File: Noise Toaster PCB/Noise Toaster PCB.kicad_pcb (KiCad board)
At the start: 2 copper layers, 170 x 97.5 mm, 133 parts, among them Q1 2N5457, Q10 2N3906, Q2 2N3904, Q3 2N3904, Q4 2N3904, Q5 2N3904, Q6 2N3904, Q7 2N5457, Q8 2N5457, Q9 2N5457, U1 LM324, U2 LM324, U3 LM386, X10 Conn_01x01_Pin, X11 Conn_01x01_Pin, X12 Conn_01x01_Pin, X13 Conn_01x01_Pin, X14 Conn_01x01_Pin, X24 Conn_01x01_Pin, X25 Conn_01x01_Pin, X26 Conn_01x01_Pin, X27 Conn_01x01_Pin, X8 Conn_01x01_Pin, X9 Conn_01x01_Pin

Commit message: created pcb file
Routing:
- net GND: track 0.00 -> 173.6 mm
- net /ARG: track 0.00 -> 90.3 mm
- net /RMP: track 0.00 -> 88.5 mm
- net /G2: track 0.00 -> 77.0 mm
- net /Attack Release Envelope Generator/X19: track 0.00 -> 73.7 mm
- net /Front Panel/B: track 0.00 -> 73.6 mm
- net /Audio Amplifier/X27: track 0.00 -> 60.0 mm
- net /Front Panel/X10: track 0.00 -> 54.5 mm
- net Net-(R39-Pad2): track 0.00 -> 46.4 mm
- net /SQR: track 0.00 -> 44.5 mm
- net Net-(Q3-C): track 0.00 -> 40.5 mm
- net Net-(U2D-+): track 0.00 -> 40.0 mm
- net /Front Panel/X5: track 0.00 -> 39.9 mm
- net /AA: track 0.00 -> 39.4 mm
- net Net-(Q3-B): track 0.00 -> 39.0 mm
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- added copper zone on F.Cu, net B+
- added copper zone on B.Cu, net B-
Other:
- board size 170 x 97.5 mm -> 168.2 x 96.5 mm

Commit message: created gerber files
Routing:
- net B+: track 37.9 -> 20.0 mm
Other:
- board text added: "Music From Outer Space LLC Design by Ray Wilson CC-BY-NC-SA"
- board text added: "Noise Toaster"
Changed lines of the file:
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@@
       (viasonmask false)
       (mode 1)
-      (useauxorigin false)
+      (useauxorigin true)
       (hpglpennumber 1)
       (hpglpenspeed 20)
@@
       (outputformat 1)
       (mirror false)
-      (drillshape 1)
+      (drillshape 0)
       (scaleselection 1)
-      (outputdirectory "")
+      (outputdirectory "Gerber Files")
     )
   )
@@
   (gr_rect (start 63.84 49.84) (end 232.09 146.34)
     (stroke (width 0.1) (type default)) (fill none) (layer "Edge.Cuts"))
+  (gr_text "Music From Outer Space LLC\nDesign by Ray Wilson\nCC-BY-NC-SA" (at 198.84 144.34) (layer "F.SilkS")
+    (effects (font (size 1 1) (thickness 0.15)) (justify left bottom))
+  )
+  (gr_text "Noise Toaster" (at 73.84 53.34) (layer "F.SilkS")
+    (effects (font (size 2 2) (thickness 0.15)) (justify left bottom))
+  )
   (segment (start 180.2 90.03) (end 175.15 90.03) (width 0.5) (layer "F.Cu") (net 1))
   (segment (start 185.255 100.215) (end 185.28 100.19) (width 0.5) (layer "F.Cu") (net 1))
@@
   (segment (start 187.3 91.3) (end 188.84 92.84) (width 0.5) (layer "F.Cu") (net 7))
   (segment (start 187.795 104.52) (end 187.795 112.14) (width 0.5) (layer "F.Cu") (net 7))
-  (segment (start 190.34 57.34) (end 190.34 57.03) (width 0.5) (layer "F.Cu") (net 8))
-  (segment (start 181.34 63.34) (end 183.34 61.34) (width 0.5) (layer "F.Cu") (net 8))
   (segment (start 179.87 65.52) (end 180.642233 65.52) (width 0.5) (layer "F.Cu") (net 8))
-  (segment (start 180.642233 65.52) (end 181.34 64.822233) (width 0.5) (layer "F.Cu") (net 8))
-  (segment (start 186.34 61.34) (end 190.34 57.34) (width 0.5) (layer "F.Cu") (net 8))
-  (segment (start 183.34 61.34) (end 186.34 61.34) (width 0.5) (layer "F.Cu") (net 8))
-  (segment (start 190.34 57.03) (end 192.9 54.47) (width 0.5) (layer "F.Cu") (net 8))
-  (segment (start 181.34 64.822233) (end 181.34 63.34) (width 0.5) (layer "F.Cu") (net 8))
   (segment (start 107.25 82.82) (end 106 84.07) (width 0.5) (layer "B.Cu") (net 8))
   (segment (start 106 84.07) (end 99.07 84.07) (width 0.5) (layer "B.Cu") (net 8))

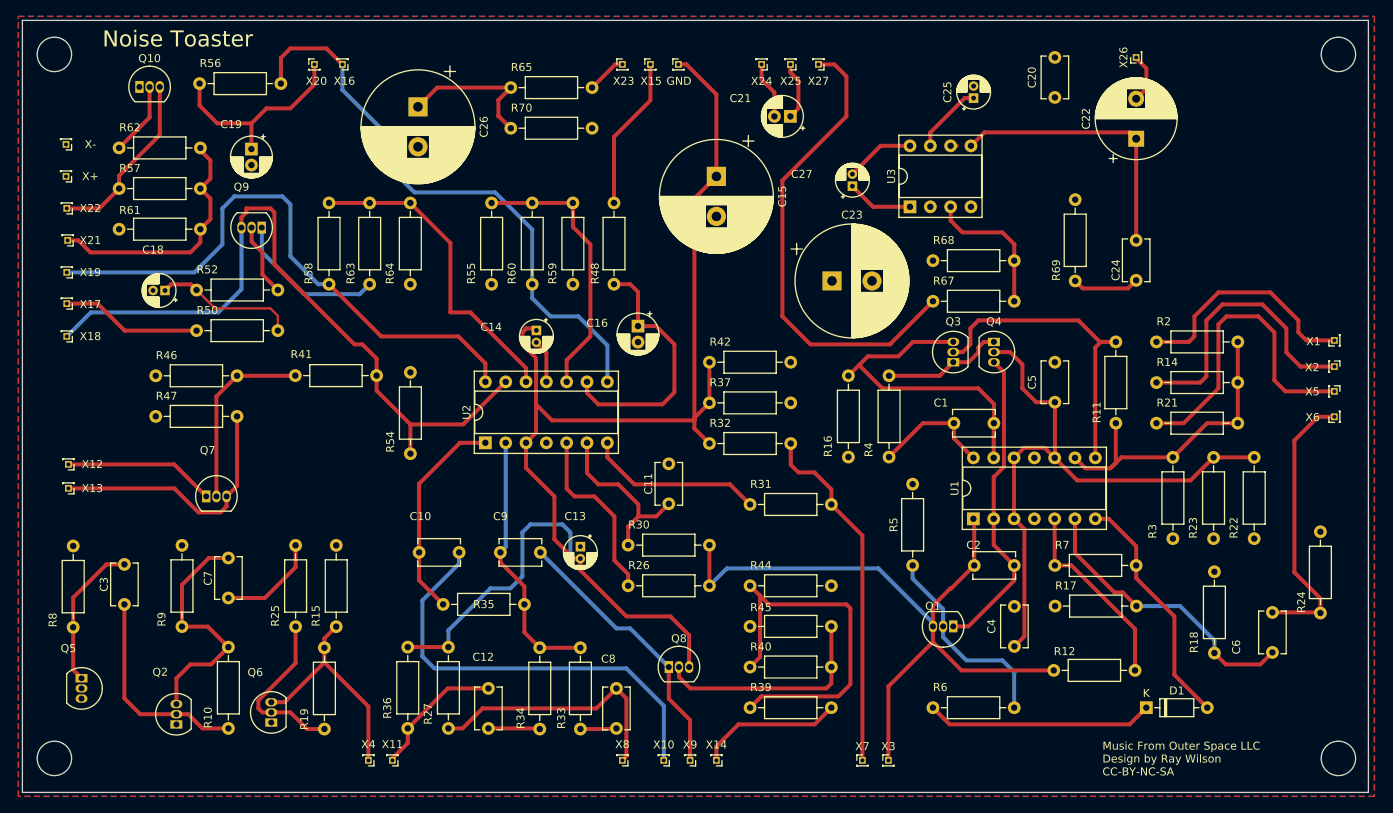
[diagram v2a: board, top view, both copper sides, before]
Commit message: rerooted some circuit paths
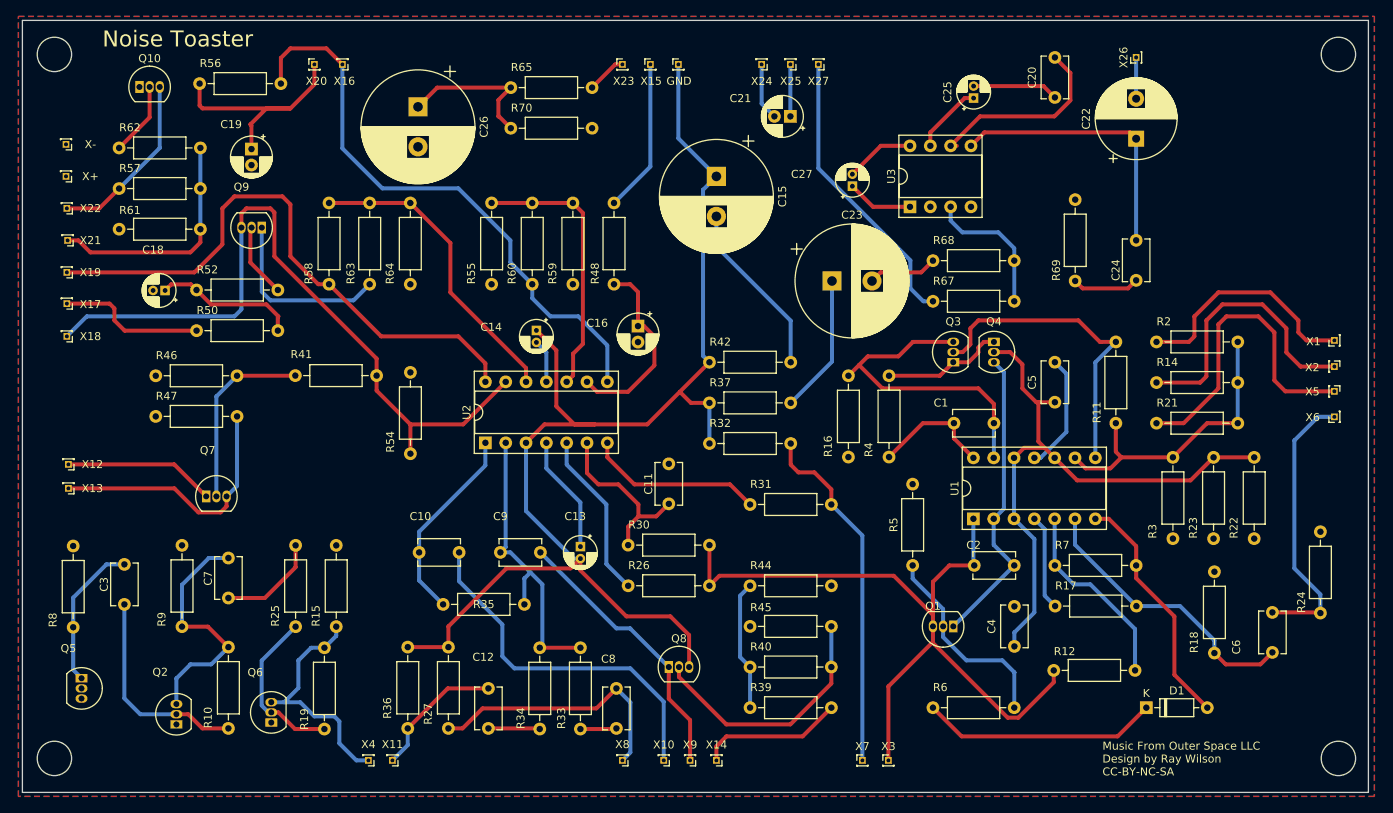
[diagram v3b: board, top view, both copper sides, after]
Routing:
- net B+: track 20.0 -> 91.2 mm
- net B-: track 5.45 -> 61.6 mm
- net Net-(R39-Pad2): track 46.4 -> 16.3 mm
- net /Audio Amplifier/X27: track 60.0 -> 36.3 mm
- net GND: track 173.6 -> 161.2 mm
- net /Front Panel/X10: track 54.5 -> 45.1 mm
- net Net-(U2C--): track 32.7 -> 24.2 mm
- net /RMP: track 88.5 -> 95.1 mm
- net Net-(U2A--): track 33.0 -> 38.3 mm
- net /Front Panel/X20: track 25.7 -> 29.9 mm
- net Net-(Q8-G): track 28.3 -> 32.0 mm
- net /Attack Release Envelope Generator/X21: track 31.9 -> 29.8 mm
- net /FO: track 26.7 -> 24.9 mm
- net /WNS: track 28.5 -> 30.1 mm
- net Net-(U2D-+): track 40.0 -> 38.5 mm
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
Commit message: changed the pcb to the original size factor
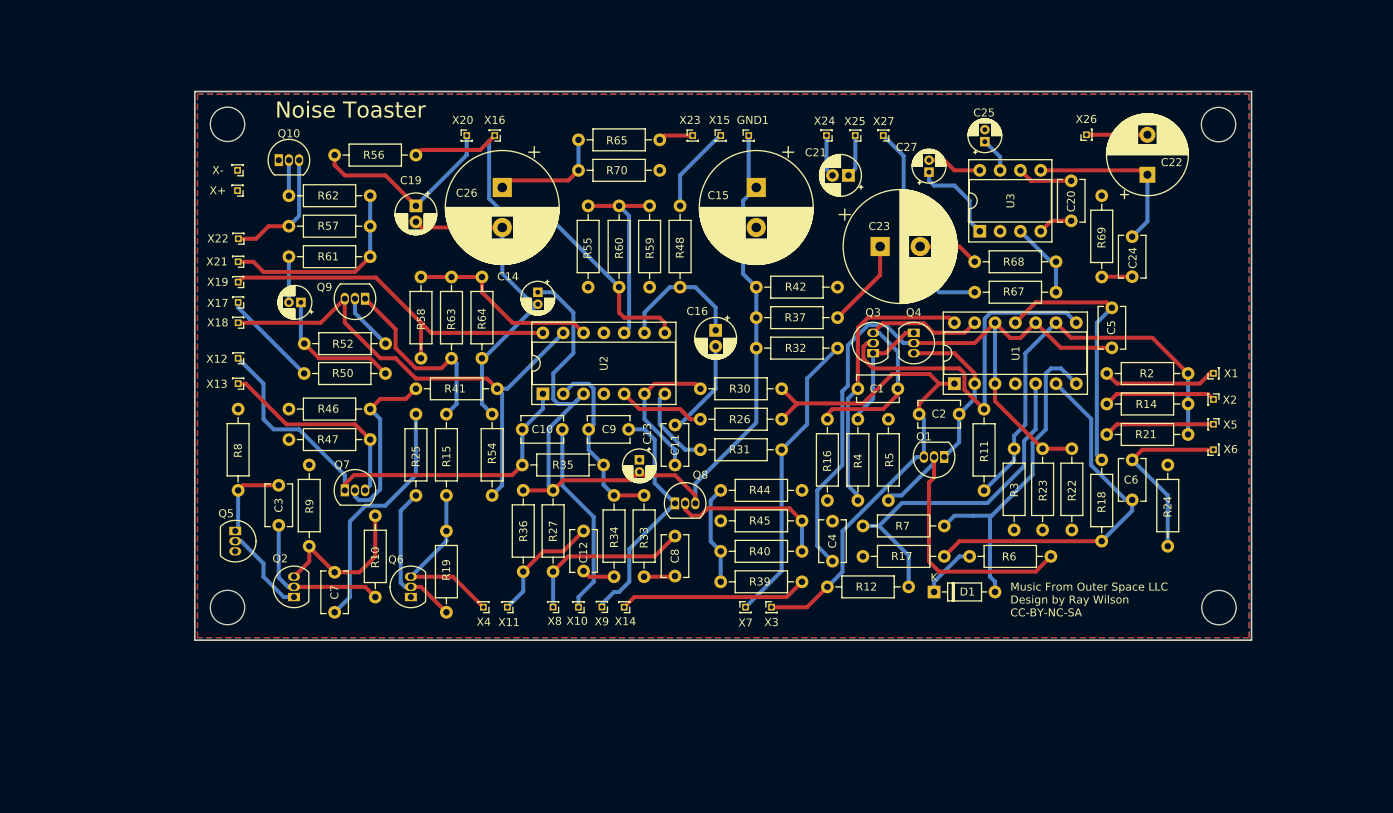
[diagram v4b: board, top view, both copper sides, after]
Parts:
- moved D1 30.2 mm to (177.8, 121.3)
- moved R12 30.2 mm to (164.5, 120.7)
- moved REF** 28.7 mm to (89.5, 123.2)
- moved R8 26.8 mm to (90.8, 98.4)
- moved Q5 26.6 mm to (90.4, 113.7)
- moved C6 25.9 mm to (202.6, 104.8)
- moved C4 25.1 mm to (165.1, 117.4)
- moved X12 25.0 mm to (90.8, 92.1)
- moved X13 24.9 mm to (90.8, 95.2)
- moved R17 24.8 mm to (179.1, 116.8)
- moved R10 24.6 mm to (108.0, 111.8)
- moved R7 24.5 mm to (168.9, 113.0)
- moved R36 24.3 mm to (126.4, 108.6)
- moved X3 24.1 mm to (157.5, 123.2)
- moved X7 24.1 mm to (154.2, 123.2)
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- renumbered GND to GND1
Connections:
- Q7 pad 1: /Front Panel/A -> /FO
- X12 pad 1: /Front Panel/A -> /FO
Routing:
- net B-: track 61.6 -> 116.5 mm
- net GND: track 161.2 -> 110.7 mm
- net B+: track 91.2 -> 42.1 mm
- net /FO: track 24.9 -> 57.8 mm
- net /Attack Release Envelope Generator/X19: track 73.7 -> 45.6 mm
- net /RMP: track 95.1 -> 67.4 mm
- net /Front Panel/X5: track 39.9 -> 13.9 mm
- net /ARG: track 91.1 -> 65.6 mm
- net /Front Panel/B: track 73.2 -> 50.6 mm
- net Net-(D1-K): track 29.6 -> 7.03 mm
- net /Front Panel/X2: track 35.4 -> 14.1 mm
- net /Front Panel/X10: track 45.1 -> 24.6 mm
- net Net-(C1-Pad2): track 15.2 -> 34.8 mm
- net Net-(U1B-+): track 24.4 -> 43.3 mm
- net /Front Panel/A: track 18.9 -> 0.00 mm
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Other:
- board size 168.2 x 96.5 mm -> 132.1 x 68.6 mm

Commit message: beautified pcb
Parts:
- moved C25 19.4 mm to (174.0, 81.5)
- moved C5 19.4 mm to (189.9, 107.3)
- moved D1 19.4 mm to (167.7, 137.8)
- moved Q3 19.4 mm to (160.1, 108.0)
- moved R21 19.4 mm to (199.4, 118.1)
- moved R3 19.4 mm to (177.7, 119.9)
- moved R33 19.4 mm to (131.4, 135.9)
- moved R4 19.4 mm to (158.1, 116.2)
- moved C14 19.4 mm to (118.1, 100.4)
- moved C26 19.4 mm to (113.7, 87.3)
- moved Q7 19.4 mm to (94.0, 125.1)
- moved Q9 19.4 mm to (96.6, 101.2)
- moved R27 19.4 mm to (120.0, 135.3)
- moved R35 19.4 mm to (116.2, 121.9)
- moved R56 19.4 mm to (102.9, 83.2)
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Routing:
- net GND: track 110.7 -> 114.1 mm
- net /Front Panel/B: track 50.6 -> 53.4 mm
- net /Front Panel/X20: track 25.0 -> 27.0 mm
- net /Front Panel/X15: track 11.0 -> 12.9 mm
- net /Audio Amplifier/X24: track 5.30 -> 7.05 mm
- net /Audio Amplifier/X27: track 26.9 -> 28.7 mm
- net /Audio Amplifier/X25: track 5.34 -> 7.08 mm
- net /Front Panel/X23: track 4.34 -> 5.88 mm
- net /Audio Amplifier/X26: track 7.62 -> 9.05 mm

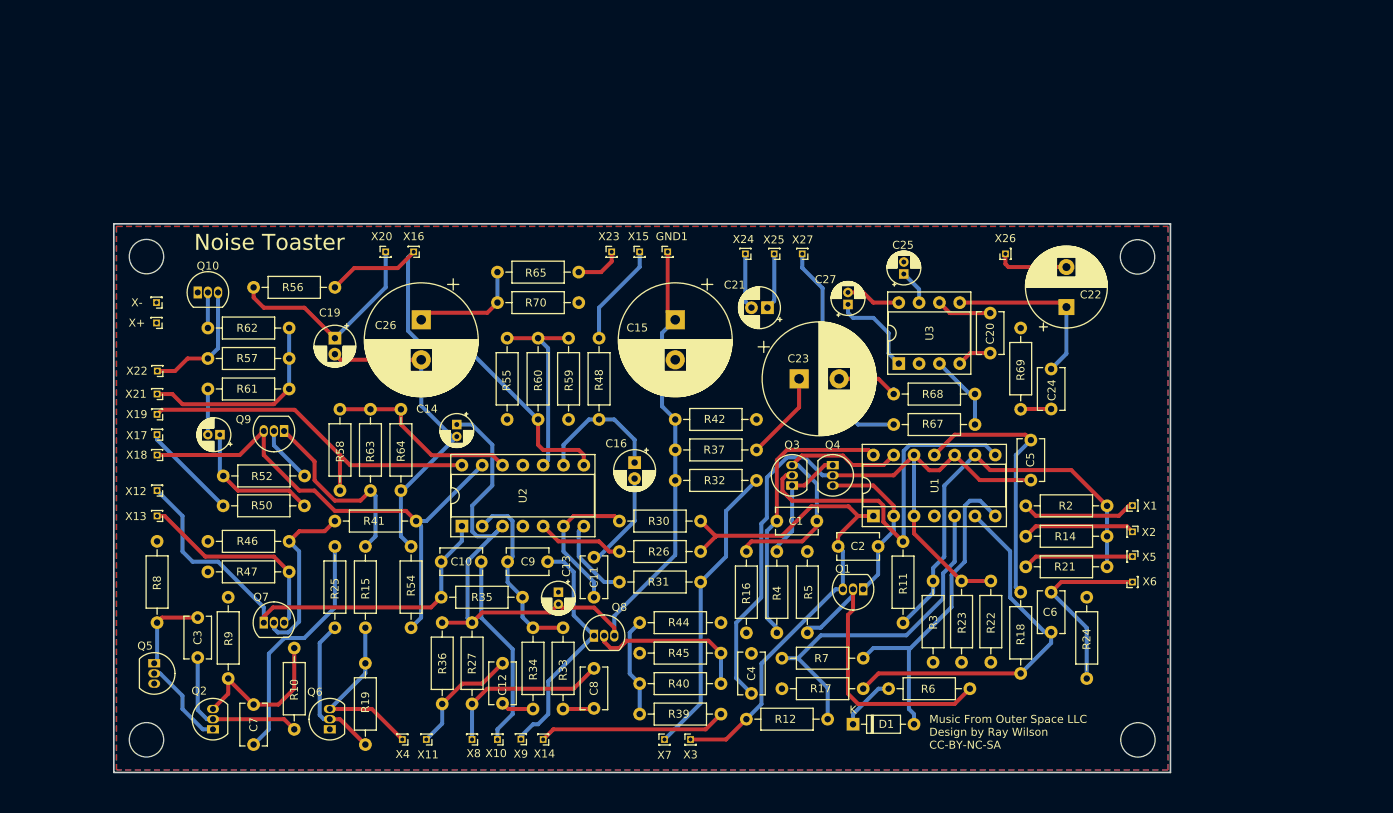
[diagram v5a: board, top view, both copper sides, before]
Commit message: changed header pins to groups
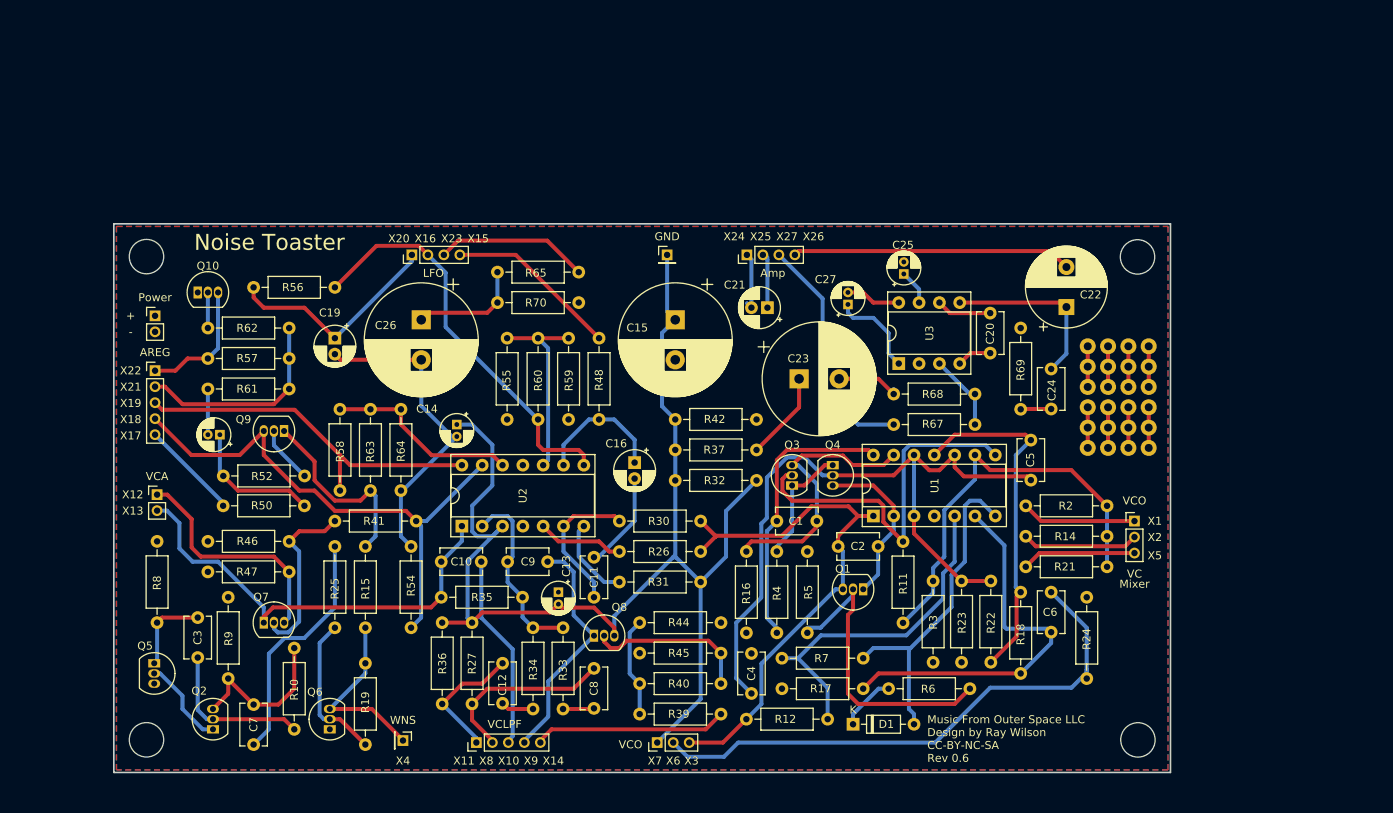
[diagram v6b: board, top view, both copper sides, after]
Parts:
- removed X+, X-, X1, X15, X16, X17, X18, X19, X2, X20, X21, X22, X23, X3, X5, X6, X7: ~, Connector_PinHeader_1.00mm:PinHeader_1x01_P1.00mm_Vertical
- removed X10, X11, X12, X13, X14, X24, X25, X26, X27, X8, X9: Conn_01x01_Pin, Connector_PinHeader_1.00mm:PinHeader_1x01_P1.00mm_Vertical
- added ?: , , F.Cu at (202.1, 103.3)
- added ?: , , F.Cu at (204.6, 90.6)
- added ?: , , F.Cu at (202.1, 98.2)
- added ?: , , F.Cu at (204.6, 93.1)
- added ?: , , F.Cu at (199.5, 93.1)
- added ?: , , F.Cu at (197.0, 100.7)
- added ?: , , F.Cu at (197.0, 103.3)
- added ?: , , F.Cu at (199.5, 95.7)
- added ?: , , F.Cu at (197.0, 93.1)
- added ?: , , F.Cu at (197.0, 98.2)
- added ?: , , F.Cu at (199.5, 90.6)
- added ?: , , F.Cu at (204.6, 98.2)
- added ?: , , F.Cu at (202.1, 93.1)
- added ?: , , F.Cu at (197.0, 95.7)
- added ?: , , F.Cu at (202.1, 90.6)
- added ?: , , F.Cu at (204.6, 100.7)
- added ?: , , F.Cu at (202.1, 100.7)
- added ?: , , F.Cu at (199.5, 98.2)
- added ?: , , F.Cu at (202.1, 95.7)
- added ?: , , F.Cu at (204.6, 95.7)
- added ?: , , F.Cu at (204.6, 103.3)
- added ?: , , F.Cu at (199.5, 100.7)
- added ?: , , F.Cu at (199.5, 103.3)
- added ?: , , F.Cu at (197.0, 90.6)
- added J2: Power, Connector_PinHeader_2.00mm:PinHeader_1x02_P2.00mm_Vertical, F.Cu at (80.4, 86.8)
- added J3: AREG, Connector_PinHeader_2.00mm:PinHeader_1x05_P2.00mm_Vertical, F.Cu at (80.4, 93.6)
- added J4: LFO, Connector_PinHeader_2.00mm:PinHeader_1x04_P2.00mm_Vertical, F.Cu at (112.5, 79.1)
- added J5: VCO, Connector_PinHeader_2.00mm:PinHeader_1x03_P2.00mm_Vertical, F.Cu at (202.8, 112.4)
- added J6: VCO, Connector_PinHeader_2.00mm:PinHeader_1x03_P2.00mm_Vertical, F.Cu at (143.2, 140.1)
- added J7: VCLPF, Connector_PinHeader_2.00mm:PinHeader_1x05_P2.00mm_Vertical, F.Cu at (120.6, 140.1)
- added J8: VCA, Connector_PinHeader_2.00mm:PinHeader_1x02_P2.00mm_Vertical, F.Cu at (80.7, 109.1)
- added J9: Amp, Connector_PinHeader_2.00mm:PinHeader_1x04_P2.00mm_Vertical, F.Cu at (154.4, 79.1)
- GND1: value ~ -> GND; footprint Connector_PinHeader_1.00mm:PinHeader_1x01_P1.00mm_Vertical -> Connector_PinHeader_2.00mm:PinHeader_1x01_P2.00mm_Vertical
- X4: value ~ -> WNS; footprint Connector_PinHeader_1.00mm:PinHeader_1x01_P1.00mm_Vertical -> Connector_PinHeader_2.00mm:PinHeader_1x01_P2.00mm_Vertical
- moved GND1 0.39 mm to (144.4, 79.1)
- moved X4 0.15 mm to (111.4, 139.9), turned to -90 degrees
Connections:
- R31 pad 2: /SQR -> GND
- R32 pad 2: /SQR -> GND
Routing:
- net /Front Panel/X6: track 23.3 -> 69.8 mm
- net GND: track 114.1 -> 156.4 mm
- net (no net): track 0.00 -> 40.6 mm
- net /SQR: track 37.2 -> 0.00 mm
- net /Audio Amplifier/X26: track 9.05 -> 35.0 mm
- net /Front Panel/X23: track 5.88 -> 19.2 mm
- net B-: track 116.5 -> 126.8 mm
- net /Front Panel/X15: track 12.9 -> 21.7 mm
- net /Front Panel/X12: track 26.0 -> 29.2 mm
- net Net-(U1B--): track 46.2 -> 48.7 mm
- net /Front Panel/B: track 53.4 -> 51.2 mm
- net /ARG: track 65.6 -> 67.8 mm
- net /FO: track 57.8 -> 56.0 mm
- net /Front Panel/X8: track 21.5 -> 22.7 mm
- net /Audio Amplifier/X27: track 28.7 -> 29.8 mm
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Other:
- board text added: "Music From Outer Space LLC Design by Ray Wilson CC-BY-NC-SA Rev 0.6"
- board text removed: "Music From Outer Space LLC Design by Ray Wilson CC-BY-NC-SA"
